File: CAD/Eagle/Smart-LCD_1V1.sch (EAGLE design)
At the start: 55 parts, among them Q121 MMBT2222AL, U101 MEGA8-P, U221 MCP4018T-104E/LT, U401 TS4871ID, X131 LDR, X141 Switches, X151 LEDs, X201 LCD_23WAY__UC1608, X231 LED_A, X232 LED_K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

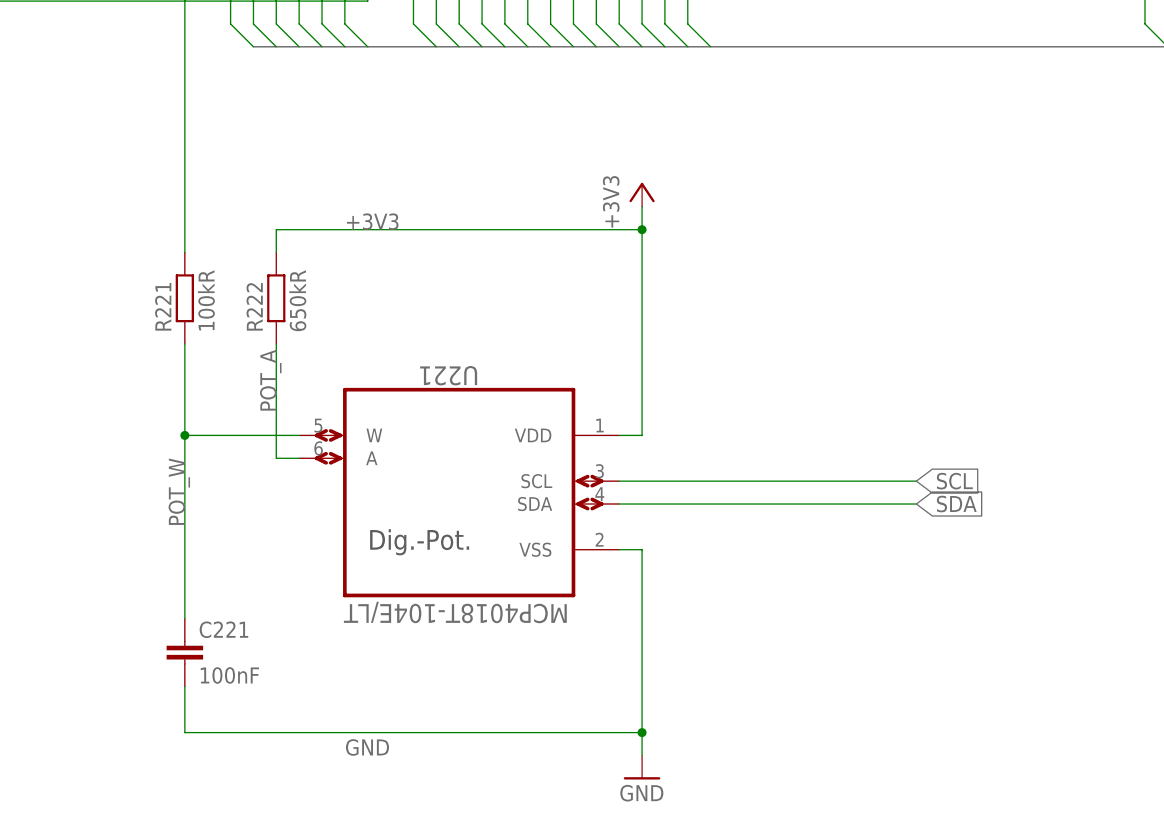
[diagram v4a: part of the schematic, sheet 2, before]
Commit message: HW_V1.1 - I2C poti removed
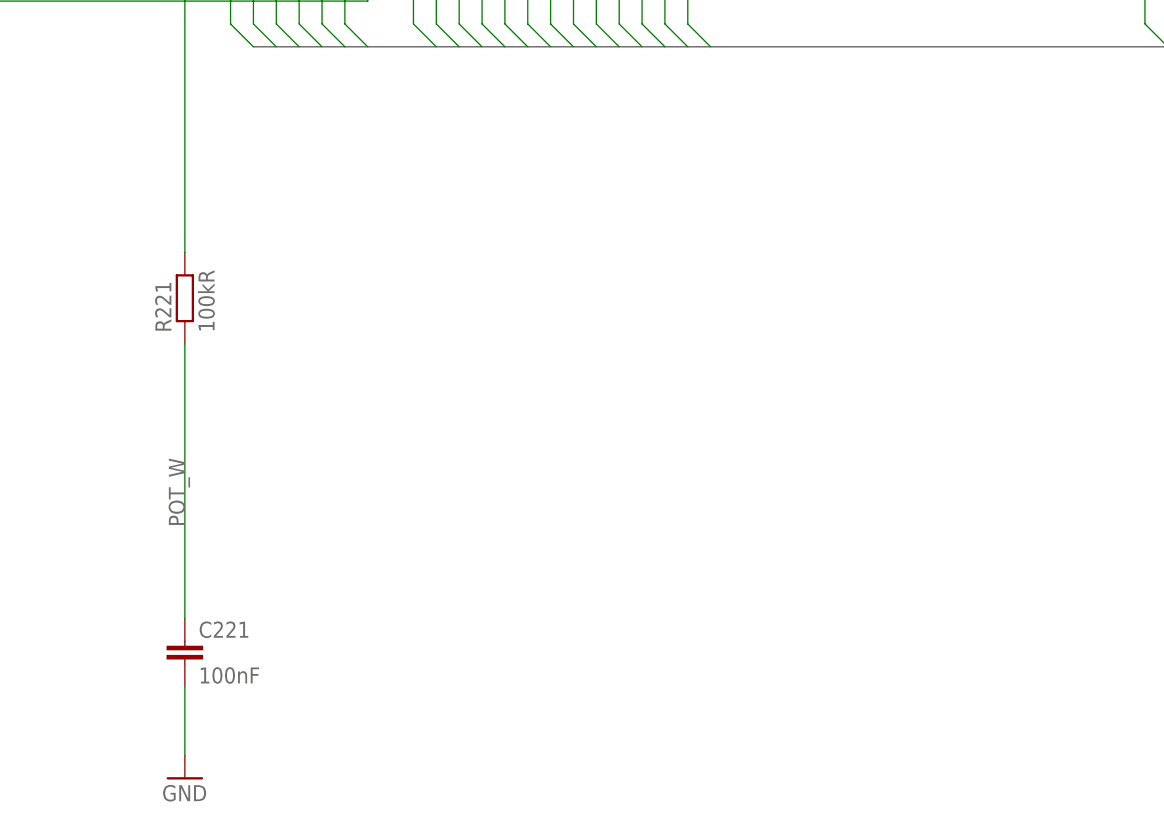
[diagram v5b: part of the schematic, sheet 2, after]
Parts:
- removed R222: 650kR, rcl:R-EU_R0805
- removed U221: MCP4018T-104E/LT, df4iah_dig-pot:MCP4018T-104E/LT
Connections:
- removed net POT_A: R222.1, U221.A
- net +3V3: no longer R222.2, U221.VDD
- net GND: no longer U221.VSS
- net POT_W: no longer U221.W
- net SCL: no longer U221.SCL
- net SDA: no longer U221.SDA
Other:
- note removed: "Dig.-Pot."
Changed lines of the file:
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@@
 <part name="C211" library="rcl" deviceset="C-EU" device="C0805" value="1uF"/>
 <part name="R211" library="rcl" deviceset="R-EU_" device="R0805" value="10MR"/>
-<part name="R222" library="rcl" deviceset="R-EU_" device="R0805" value="650kR"/>
 <part name="R221" library="rcl" deviceset="R-EU_" device="R0805" value="100kR"/>
 <part name="C221" library="rcl" deviceset="C-EU" device="C0805" value="100nF"/>
-<part name="U221" library="df4iah_dig-pot" deviceset="MCP4018T-104E/LT" device=""/>
 <part name="C302" library="rcl" deviceset="C-EU" device="C0805" value="100nF"/>
 <part name="C301" library="rcl" deviceset="C-EU" device="C0805" value="100nF"/>
@@
 <part name="+5V0_241" library="df4iah_supply" deviceset="+5V" device=""/>
 <part name="GND121" library="df4iah_supply" deviceset="GND" device=""/>
-<part name="+3V3_221" library="df4iah_supply" deviceset="+3V3" device=""/>
 <part name="X131" library="df4iah_connector" deviceset="HEADER-1X2" device="" value="LDR"/>
 <part name="+3V3_131" library="df4iah_supply" deviceset="+3V3" device=""/>
@@
 <description>LCD panel</description>
 <plain>
-<text x="116.84" y="45.72" size="2.1844" layer="97" ratio="12">Dig.-Pot.</text>
 <text x="157.48" y="121.92" size="1.778" layer="97" rot="R90">BM1</text>
 <text x="154.94" y="121.92" size="1.778" layer="97" rot="R90">BM0</text>
@@
 <instance part="C211" gate="G$1" x="48.26" y="91.44"/>
 <instance part="R211" gate="G$1" x="35.56" y="91.44" rot="R90"/>
-<instance part="R222" gate="G$1" x="106.68" y="73.66" rot="R90"/>
 <instance part="R221" gate="G$1" x="96.52" y="73.66" rot="R90"/>
 <instance part="C221" gate="G$1" x="96.52" y="35.56"/>
-<instance part="U221" gate="A" x="127" y="55.88" smashed="yes" rot="MR0">
-<attribute name="NAME" x="122.428" y="66.0908" size="2.0828" layer="95" ratio="10" rot="SMR180"/>
-<attribute name="VALUE" x="114.1984" y="39.6748" size="2.0828" layer="96" ratio="10" rot="SMR180"/>
-</instance>
-<instance part="GND221" gate="1" x="147.32" y="20.32"/>
+<instance part="GND221" gate="1" x="96.52" y="20.32"/>
 <instance part="GND211" gate="1" x="58.42" y="68.58"/>
 <instance part="+3V3_201" gate="G$1" x="35.56" y="134.62"/>
 <instance part="+5V0_241" gate="G$1" x="187.96" y="134.62"/>
-<instance part="+3V3_221" gate="G$1" x="147.32" y="86.36"/>
 <instance part="X232" gate="G$1" x="203.2" y="139.7" rot="R90"/>
 <instance part="X231" gate="G$1" x="193.04" y="139.7" rot="R90"/>
@@
 </segment>
 </net>
-<net name="POT_A" class="0">
-<segment>
-<pinref part="R222" gate="G$1" pin="1"/>
-<wire x1="106.68" y1="68.58" x2="106.68" y2="55.88" width="0.1524" layer="91"/>
-<pinref part="U221" gate="A" pin="A"/>
-<wire x1="106.68" y1="55.88" x2="109.22" y2="55.88" width="0.1524" layer="91"/>
-<label x="106.68" y="60.96" size="1.778" layer="95" rot="R90"/>
-</segment>
-</net>
 <net name="POT_W" class="0">
 <segment>
 <pinref part="C221" gate="G$1" pin="1"/>
 <pinref part="R221" gate="G$1" pin="1"/>
-<wire x1="96.52" y1="38.1" x2="96.52" y2="58.42" width="0.1524" layer="91"/>
-<pinref part="U221" gate="A" pin="W"/>
-<wire x1="96.52" y1="58.42" x2="96.52" y2="68.58" width="0.1524" layer="91"/>
-<wire x1="96.52" y1="58.42" x2="109.22" y2="58.42" width="0.1524" layer="91"/>
-<junction x="96.52" y="58.42"/>
+<wire x1="96.52" y1="38.1" x2="96.52" y2="68.58" width="0.1524" layer="91"/>
 <label x="96.52" y="48.26" size="1.778" layer="95" rot="R90"/>
 </segment>
 </net>
-<net name="SCL" class="0">
-<segment>
-<pinref part="U221" gate="A" pin="SCL"/>
-<wire x1="144.78" y1="53.34" x2="177.8" y2="53.34" width="0.1524" layer="91"/>
-<label x="177.8" y="53.34" size="1.778" layer="95" xref="yes"/>
-</segment>
-</net>
-<net name="SDA" class="0">
-<segment>
-<pinref part="U221" gate="A" pin="SDA"/>
-<wire x1="144.78" y1="50.8" x2="177.8" y2="50.8" width="0.1524" layer="91"/>
-<label x="177.8" y="50.8" size="1.778" layer="95" xref="yes"/>
-</segment>
-</net>
 <net name="GND" class="0">
 <segment>
-<pinref part="U221" gate="A" pin="VSS"/>
-<wire x1="147.32" y1="45.72" x2="144.78" y2="45.72" width="0.1524" layer="91"/>
-<wire x1="147.32" y1="25.4" x2="147.32" y2="45.72" width="0.1524" layer="91"/>
 <pinref part="GND221" gate="1" pin="GND"/>
-<wire x1="147.32" y1="22.86" x2="147.32" y2="25.4" width="0.1524" layer="91"/>
-<junction x="147.32" y="25.4"/>
 <pinref part="C221" gate="G$1" pin="2"/>
-<wire x1="96.52" y1="25.4" x2="96.52" y2="30.48" width="0.1524" layer="91"/>
-<wire x1="96.52" y1="25.4" x2="147.32" y2="25.4" width="0.1524" layer="91"/>
-<label x="114.3" y="22.86" size="1.778" layer="95"/>
+<wire x1="96.52" y1="22.86" x2="96.52" y2="30.48" width="0.1524" layer="91"/>
 </segment>
 <segment>
@@
 <junction x="119.38" y="116.84"/>
 </segment>
-<segment>
-<pinref part="U221" gate="A" pin="VDD"/>
-<wire x1="147.32" y1="81.28" x2="147.32" y2="58.42" width="0.1524" layer="91"/>
-<wire x1="147.32" y1="58.42" x2="144.78" y2="58.42" width="0.1524" layer="91"/>
-<pinref part="R222" gate="G$1" pin="2"/>
-<wire x1="106.68" y1="78.74" x2="106.68" y2="81.28" width="0.1524" layer="91"/>
-<wire x1="106.68" y1="81.28" x2="147.32" y2="81.28" width="0.1524" layer="91"/>
-<junction x="147.32" y="81.28"/>
-<label x="114.3" y="81.28" size="1.778" layer="95"/>
-<pinref part="+3V3_221" gate="G$1" pin="+3V3"/>
-<wire x1="147.32" y1="83.82" x2="147.32" y2="81.28" width="0.1524" layer="91"/>
-</segment>
-</net>
+</net>

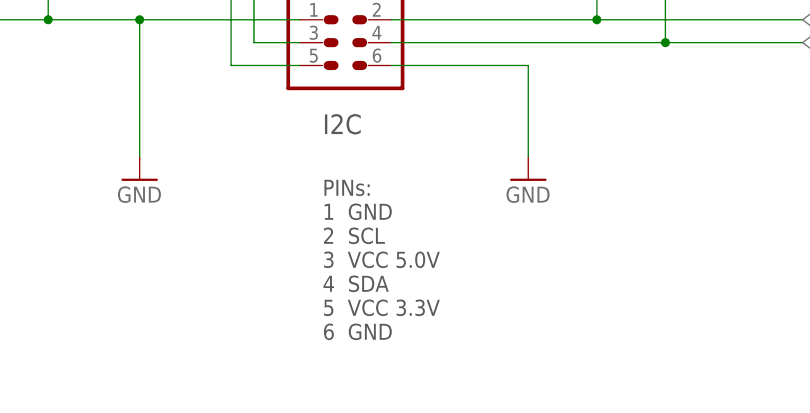
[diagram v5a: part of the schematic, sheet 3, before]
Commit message: HW_V1.1 - suggestions of Hans, DK1NB added
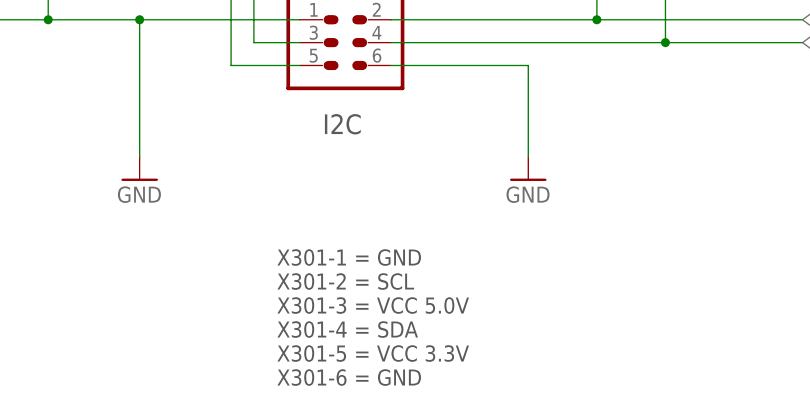
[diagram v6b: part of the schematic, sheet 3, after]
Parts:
- R132: value 1MR -> 270kR
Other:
- note added: "X131-1 = SFH203, cathode X131-2 = SFH203, anode"
- note added: "X141-1 = GND X141-2 = RotEnc-I X141-3 = PushBut X141-4 = RotEnc-Q"
- note added: "X151-1 = GND, LED cathodes X151-2 = LED red, anode X151-3 = LED green, anode"
- note added: "X301-1 = GND X301-2 = SCL X301-3 = VCC 5.0V X301-4 = SDA X301-5 = VCC 3.3V X301-6 = GND"
- note added: "X411-1 = Spk left + (8 ohms) X411-2 = Spk left - (8 ohms) X411-3 = N.C. X411-4 = N.C."
- note removed: "PINs: 1 GND 2 SCL 3 VCC 5.0V 4 SDA 5 VCC 3.3V 6 GND"
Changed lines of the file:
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@@
 <part name="C455" library="rcl" deviceset="C-EU" device="C0805" value="470nF"/>
 <part name="C452" library="rcl" deviceset="C-EU" device="C0805" value="470pF"/>
-<part name="R132" library="rcl" deviceset="R-EU_" device="R0805" value="1MR"/>
+<part name="R132" library="rcl" deviceset="R-EU_" device="R0805" value="270kR"/>
 <part name="FM502" library="df4iah_fiducial" deviceset="FIDUCIAL_MARK_1MM" device=""/>
 <part name="FM501" library="df4iah_fiducial" deviceset="FIDUCIAL_MARK_1MM" device=""/>
@@
 <text x="200.152" y="73.66" size="1.778" layer="97">RD/!WR</text>
 <text x="200.152" y="71.12" size="1.778" layer="97">EN</text>
+<text x="198.12" y="162.56" size="1.778" layer="97">X131-1 = SFH203, cathode
+X131-2 = SFH203, anode</text>
+<text x="10.16" y="142.24" size="1.778" layer="97">X151-1 = GND, LED cathodes
+X151-2 = LED red,   anode
+X151-3 = LED green, anode</text>
+<text x="127" y="162.56" size="1.778" layer="97">X141-1 = GND
+X141-2 = RotEnc-I
+X141-3 = PushBut
+X141-4 = RotEnc-Q</text>
 </plain>
 <instances>
@@
 <plain>
 <text x="121.92" y="91.44" size="2.1844" layer="97" ratio="12">I2C</text>
-<text x="121.92" y="68.58" size="1.778" layer="97">PINs:
-1  GND
-2  SCL
-3  VCC 5.0V
-4  SDA
-5  VCC 3.3V
-6  GND</text>
+<text x="116.84" y="63.5" size="1.778" layer="97">X301-1 = GND
+X301-2 = SCL
+X301-3 = VCC 5.0V
+X301-4 = SDA
+X301-5 = VCC 3.3V
+X301-6 = GND</text>
 </plain>
 <instances>
@@
 <plain>
 <text x="192.024" y="125.476" size="2.1844" layer="97" ratio="12">Audio</text>
+<text x="190.5" y="147.32" size="1.778" layer="97">X411-1 = Spk left +  (8 ohms)
+X411-2 = Spk left -  (8 ohms)
+X411-3 = N.C.
+X411-4 = N.C.</text>
 </plain>
 <instances>

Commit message: HW_V1.1 - LCD backlight - 1 ohms added to the NPN's emitter
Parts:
- added R122: 1R, rcl:R-EU_R0805
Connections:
- new net LED_PWM_E: Q121.E, R122.1
- net GND: now also R122.2; no longer Q121.E
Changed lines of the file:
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@@
 <part name="FM504" library="df4iah_fiducial" deviceset="FIDUCIAL_MARK_1MM" device=""/>
 <part name="D131" library="df4iah_diode" deviceset="BAS70-04" device="" value="BZX84-C2V4"/>
+<part name="R122" library="rcl" deviceset="R-EU_" device="R0805" value="1R"/>
 </parts>
 <sheets>
@@
 <instance part="R121" gate="G$1" x="160.02" y="86.36"/>
 <instance part="Q121" gate="G$1" x="182.88" y="86.36"/>
-<instance part="GND121" gate="1" x="185.42" y="78.74"/>
+<instance part="GND121" gate="1" x="213.36" y="78.74"/>
 <instance part="X131" gate="A" x="200.66" y="149.86"/>
 <instance part="+3V3_131" gate="G$1" x="154.94" y="154.94"/>
@@
 <attribute name="VALUE" x="188.722" y="135.7376" size="1.778" layer="96"/>
 </instance>
+<instance part="R122" gate="G$1" x="203.2" y="81.28"/>
 </instances>
 <busses>
@@
 <nets>
 <net name="GND" class="0">
-<segment>
-<pinref part="Q121" gate="G$1" pin="E"/>
-<pinref part="GND121" gate="1" pin="GND"/>
-</segment>
 <segment>
 <pinref part="C131" gate="G$1" pin="2"/>
@@
 <pinref part="C111" gate="G$1" pin="2"/>
 <pinref part="GND111" gate="1" pin="GND"/>
+</segment>
+<segment>
+<pinref part="GND121" gate="1" pin="GND"/>
+<pinref part="R122" gate="G$1" pin="2"/>
+<wire x1="213.36" y1="81.28" x2="208.28" y2="81.28" width="0.1524" layer="91"/>
 </segment>
 </net>
@@
 </segment>
 </net>
+<net name="LED_PWM_E" class="0">
+<segment>
+<pinref part="R122" gate="G$1" pin="1"/>
+<pinref part="Q121" gate="G$1" pin="E"/>
+<wire x1="198.12" y1="81.28" x2="185.42" y2="81.28" width="0.1524" layer="91"/>
+<label x="182.88" y="78.74" size="1.778" layer="95"/>
+</segment>
+</net>

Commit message: HW_V1.1 - df4iah_connector.lbr combined for Smart-LCD and FindMeSAT (2)
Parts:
- R122: value 1R -> 3R3
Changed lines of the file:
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@@
 <part name="FM504" library="df4iah_fiducial" deviceset="FIDUCIAL_MARK_1MM" device=""/>
 <part name="D131" library="df4iah_diode" deviceset="BAS70-04" device="" value="BZX84-C2V4"/>
-<part name="R122" library="rcl" deviceset="R-EU_" device="R0805" value="1R"/>
+<part name="R122" library="rcl" deviceset="R-EU_" device="R0805" value="3R3"/>
 </parts>
 <sheets>
